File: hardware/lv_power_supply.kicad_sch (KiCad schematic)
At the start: 13 parts, among them IC1 L7812ABV, Q1 PMOS, Q2 PMOS

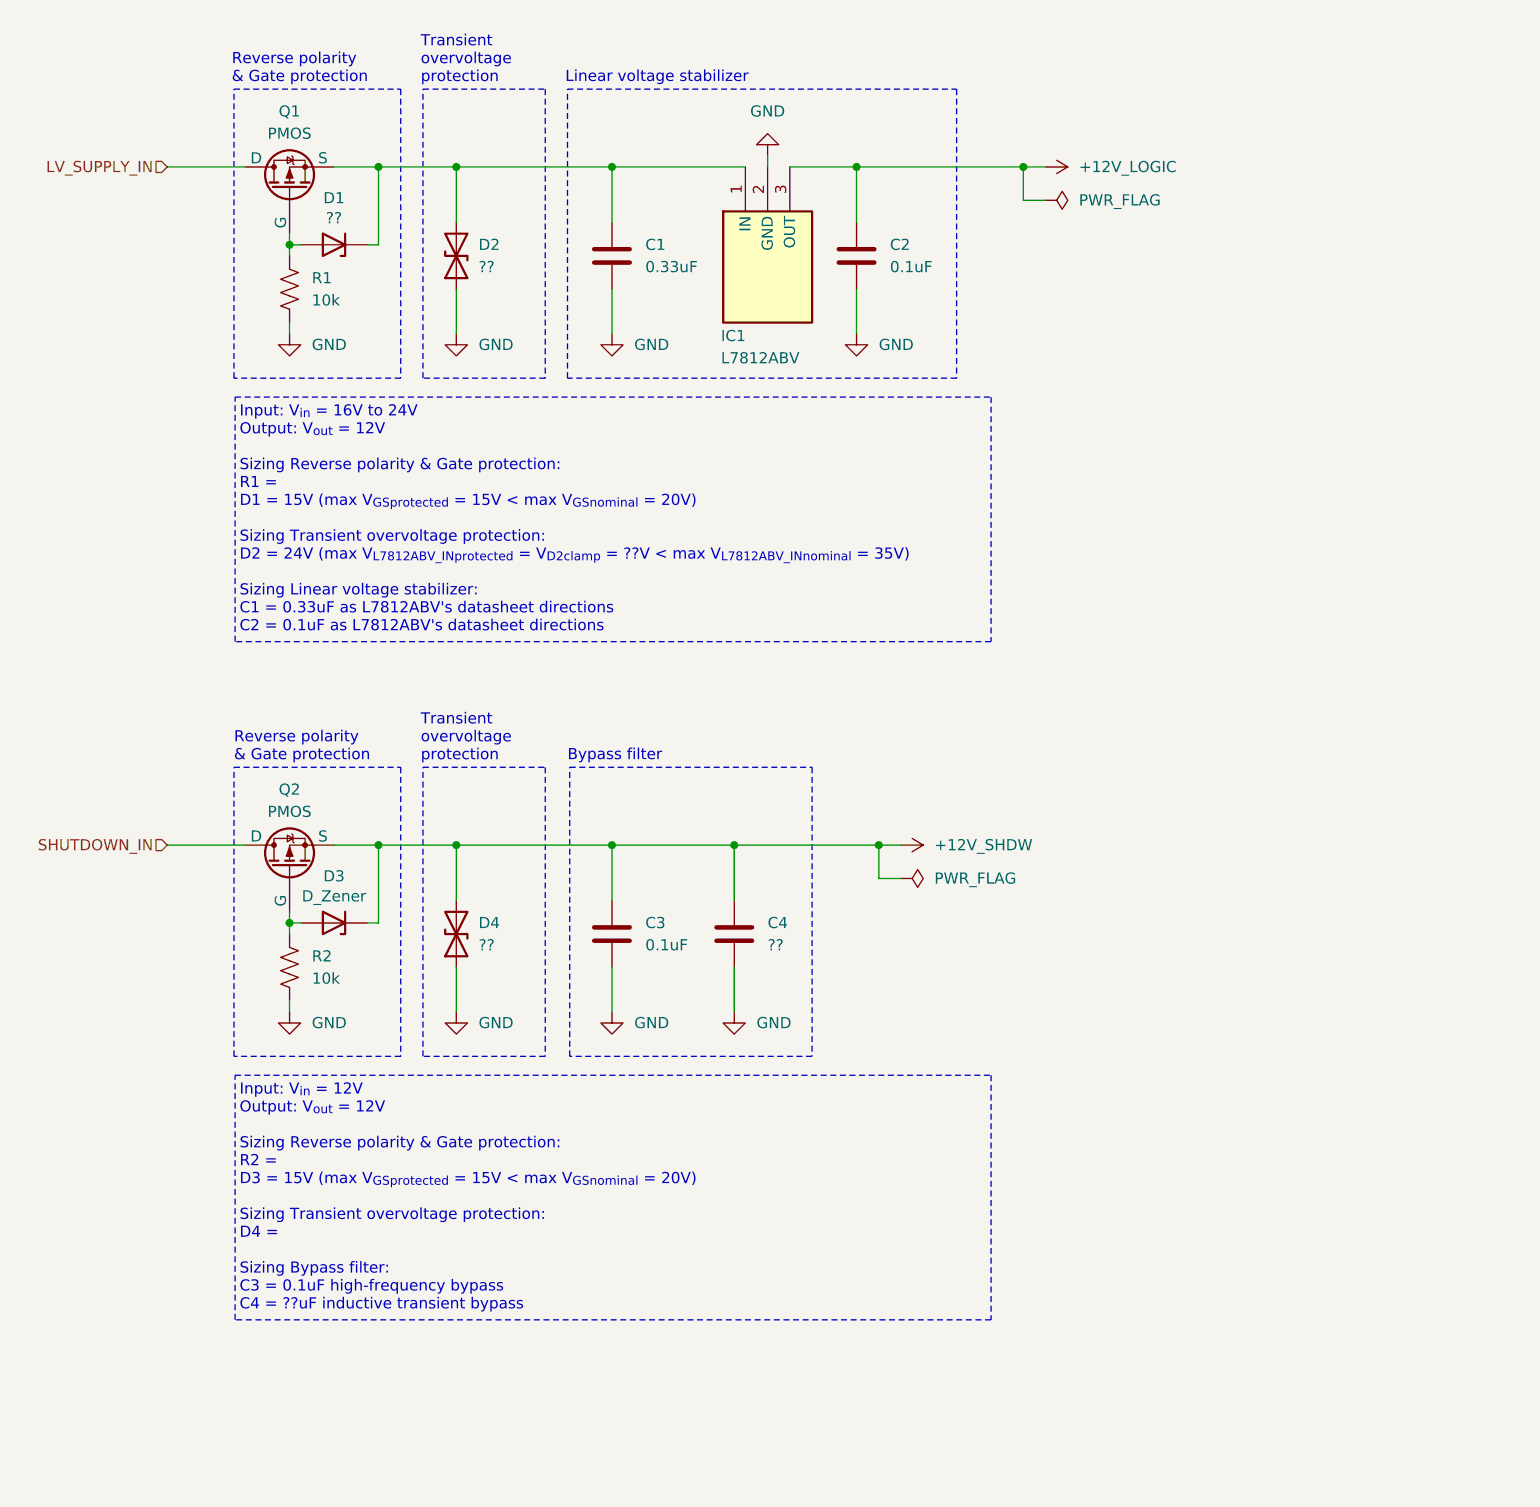
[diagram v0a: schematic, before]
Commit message: complete hierarchial sheet organization; start hv_sense schematic; start lv_logic schematic; refactor hierarchial sheets
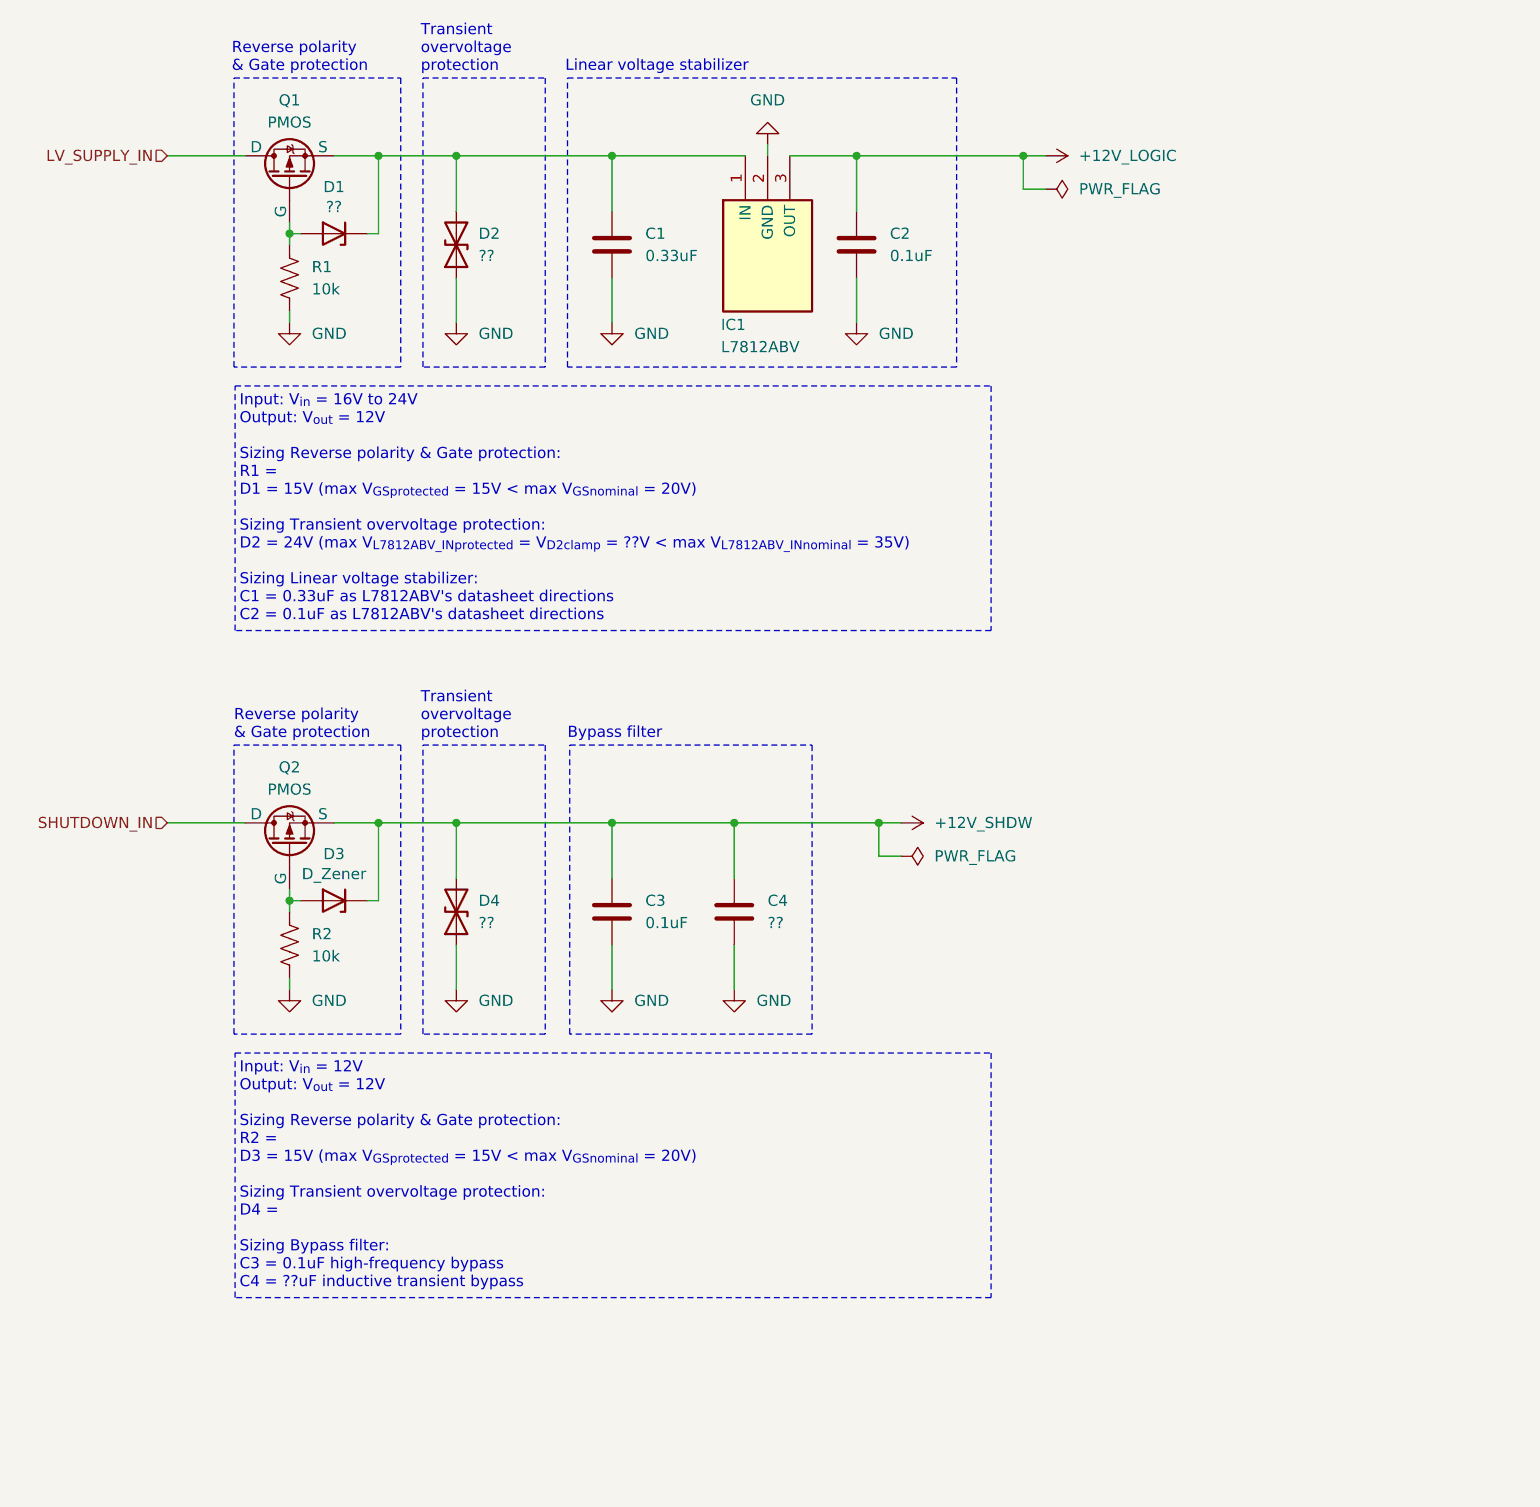
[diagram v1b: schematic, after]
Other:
- moved on the sheet: C1, C2, C3, C4, D1, D2, D3, D4, IC1, Q1, Q2, R1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

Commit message: refactor project layout merging high and low voltage in the same pcb
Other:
- note added: "Input: V_{in} = 12V Output: V_{out} = 12V Sizing Reverse polarity & Gate protection: R2 = D3 = 15V (max V_{GS}_{protected} = 15V < max V_{GS}_{nominal} = 20V) Sizing Transient overvoltage protection: D4 = Sizing Bypass filter: C3 = 0.1uF high-frequency bypass (multilayer ceramic) C4 = ??uF inductive transient bypass (multilayer ceramic)"
- note removed: "Input: V_{in} = 12V Output: V_{out} = 12V Sizing Reverse polarity & Gate protection: R2 = D3 = 15V (max V_{GS}_{protected} = 15V < max V_{GS}_{nominal} = 20V) Sizing Transient overvoltage protection: D4 = Sizing Bypass filter: C3 = 0.1uF high-frequency bypass C4 = ??uF inductive transient bypass"
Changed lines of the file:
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@@
 		)
 	)
-	(text "Input: V_{in} = 12V\nOutput: V_{out} = 12V\n\nSizing Reverse polarity & Gate protection:\nR2 = \nD3 = 15V (max V_{GS}_{protected} = 15V < max V_{GS}_{nominal} = 20V)\n\nSizing Transient overvoltage protection:\nD4 = \n\nSizing Bypass filter:\nC3 = 0.1uF high-frequency bypass\nC4 = ??uF inductive transient bypass\n"
+	(text "Input: V_{in} = 12V\nOutput: V_{out} = 12V\n\nSizing Reverse polarity & Gate protection:\nR2 = \nD3 = 15V (max V_{GS}_{protected} = 15V < max V_{GS}_{nominal} = 20V)\n\nSizing Transient overvoltage protection:\nD4 = \n\nSizing Bypass filter:\nC3 = 0.1uF high-frequency bypass (multilayer ceramic)\nC4 = ??uF inductive transient bypass (multilayer ceramic)\n"
 		(exclude_from_sim no)
 		(at 46.355 137.795 0)

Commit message: fix ERC power line errors
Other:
- moved on the sheet: C1, C2, D2, IC1

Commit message: start power supply and logic sizing
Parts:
- removed D4: ??, symbol Device:D_TVS
- removed Q1, Q2: PMOS, symbol Simulation_SPICE:PMOS
- added D13: 28V, symbol Device:D_TVS
- added Q1, Q2: SI3437DV-T1-GE3, SOT95P284X110-6N, symbol Libary_Loader:SI3437DV-T1-GE3
- added R28, R29: R_US, symbol Device:R_US
- D1: value ?? -> 15V
- D2: value ?? -> 28V
- D3: value D_Zener -> 15V
- IC1: footprint TO255P460X1020X2008-3P -> Library_Loader:TO255P460X1020X2008-3P
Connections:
- net +12V_SHDW: now also D13.2 (A2), R29.2; no longer D3.1 (K)
- net GND: now also D13.1 (A1)
- net LV_SUPPLY_IN: now also Q1.1 (D_1), Q1.2 (D_2)
- net SHUTDOWN_IN: now also Q2.1 (D_1), Q2.2 (D_2)
- net at D3.2 (A), R2.1: now also Q2.3 (G)
- net at C1.1, D2.2 (A2), IC1.1 (IN): now also R28.2; no longer D1.1 (K)
- net at D1.2 (A), R1.1: now also Q1.3 (G)
- new net: D1.1 (K), Q1.4 (S), R28.1
- new net: Q1.5 (D_3), Q1.6 (D_4)
- new net: D3.1 (K), Q2.4 (S), R29.1
- new net: Q2.5 (D_3), Q2.6 (D_4)
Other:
- note added: "Input: V_{in} = 12V Output: V_{out} = 12V Sizing Reverse polarity & Gate protection: R2 = D3 = 15V (max V_{GS}_{protected} = 15V < max V_{GS}_{nominal} = 20V) Sizing Transient overvoltage protection: R29 = D4 = Sizing Bypass filter: C3 = 0.1uF high-frequency bypass (multilayer ceramic) C4 = ??uF inductive transient bypass (multilayer ceramic)"
- note added: "Input: V_{in} = 16V to 24V Output: V_{out} = 12V Max current draw: < 1mA Sizing Reverse polarity & Gate protection: Q1: R1 = 10K (max D1 = 15V (max V_{GS}_{protected} = 15V < max V_{GS}_{nominal} = 20V) Sizing Transient overvoltage protection: R28 = D2 = 28V (max V_{L7812ABV_IN}_{protected} = V_{D2}_{clamp} = 28V < max V_{L7812ABV_IN}_{nominal} = 35V) Sizing Linear voltage stabilizer: C1 = 0.33uF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"
- note removed: "Input: V_{in} = 12V Output: V_{out} = 12V Sizing Reverse polarity & Gate protection: R2 = D3 = 15V (max V_{GS}_{protected} = 15V < max V_{GS}_{nominal} = 20V) Sizing Transient overvoltage protection: D4 = Sizing Bypass filter: C3 = 0.1uF high-frequency bypass (multilayer ceramic) C4 = ??uF inductive transient bypass (multilayer ceramic)"
- note removed: "Input: V_{in} = 16V to 24V Output: V_{out} = 12V Sizing Reverse polarity & Gate protection: R1 = D1 = 15V (max V_{GS}_{protected} = 15V < max V_{GS}_{nominal} = 20V) Sizing Transient overvoltage protection: D2 = 24V (max V_{L7812ABV_IN}_{protected} = V_{D2}_{clamp} = ??V < max V_{L7812ABV_IN}_{nominal} = 35V) Sizing Linear voltage stabilizer: C1 = 0.33uF as L7812ABV's datasheet directions C2 = 0.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"
- moved on the sheet: C1, C2, C3, C4, D1, D2, IC1, R1
